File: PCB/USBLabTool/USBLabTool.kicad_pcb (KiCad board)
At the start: 4 copper layers, 79.4 x 56.2 mm, 232 parts, among them J1 Conn_01x06_Pin, J10 T_pwm, J11 T_buf, J12 T_buf, J13 ADC2, J14 ADC1, J15 +3.3VA, J16 +3.3VA, J17 2x01, J19 T_N5V, J2 Conn_02x12_Odd_Even, J20 USB_C_Receptacle, J3 T_att, J4 T_att, J5 T_acdc, J6 T_acdc, J7 T_amp, J8 T_amp, J9 T_pwm, K1 G5V-2, K2 G5V-2, Q1 STL11N3LLH6, SW1 SW_Push, U1 AQY284SX, U10 Opamp_Quad, U11 DG403, U12 STM32H562VGTx, U13 r1283, U14 ST1L05APU33R, U15 ST1L05APU33R, U16 LTC1983ES6-5#TRPBF, U17 TCPP01-M12, U18 74HC245, U2 AQY284SX, U20 74HC245, U3 CD74HC4316PWR, U4 LMP7718, U5 CD74HC4316PWR, U6 LMP7718, U7 OPA863, U8 OPA863, U9 Opamp_Quad, Y1 32.768kHz

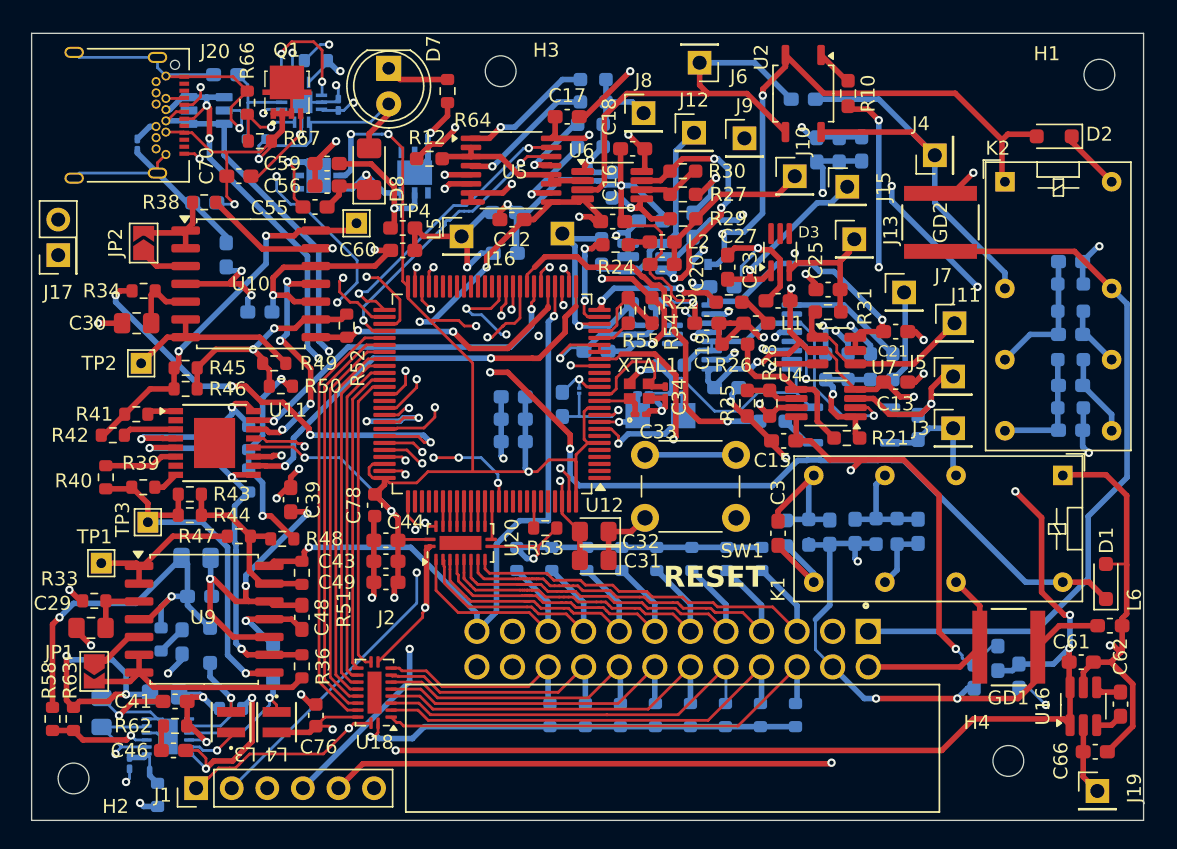
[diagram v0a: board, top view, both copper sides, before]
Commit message: fix footprint and change button
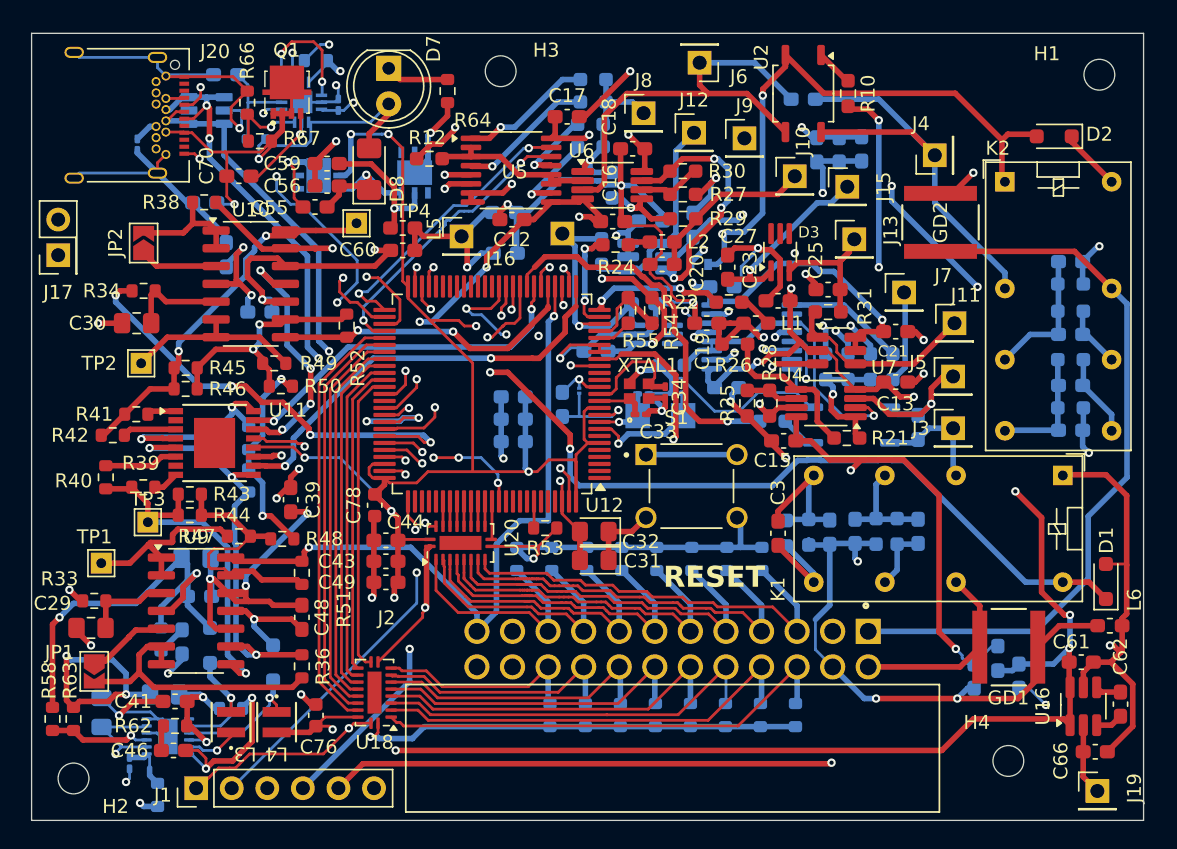
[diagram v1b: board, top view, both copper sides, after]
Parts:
- removed SW1: SW_Push, Button_Switch_THT:SW_PUSH_6mm_H7.3mm
- added S1: TS02-66-73-BK-100-SCR-D, userfp:SW_TS02-66-73-BK-100-SCR-D, F.Cu at (157.1, 97.9)
- U10, U9: footprint Package_SO:SOIC-14W_7.5x9mm_P1.27mm -> Package_SO:SOIC-14_3.9x8.7mm_P1.27mm
- moved U9 0.83 mm to (121.8, 106.8)
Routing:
- net Net-(U9D--): track 13.8 -> 19.0 mm
- net Net-(JP1-B): track 17.1 -> 20.2 mm
- net DAC1_OUT1: track 47.0 -> 49.7 mm
- net +12VA: track 82.3 -> 84.5 mm
- net DAC1_OUT2: track 45.9 -> 48.1 mm
- net Net-(U10B-+): track 4.92 -> 7.10 mm
- net /AWG_FrontEnd/C1_IN: track 3.38 -> 5.56 mm
- net /AWG_FrontEnd/C0_FB: track 28.2 -> 30.3 mm
- net Net-(JP2-B): track 6.56 -> 8.44 mm
- net /AWG_FrontEnd/C0_V_OFF: track 11.2 -> 13.1 mm
- net /AWG_FrontEnd/C0_IN: track 3.92 -> 5.77 mm
- net Net-(U9A-+): track 4.33 -> 6.17 mm
- net GND: track 307.7 -> 309.5 mm
- net -12VA: track 74.5 -> 75.3 mm
- net Net-(U10C--): track 16.9 -> 17.7 mm
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
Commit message: PCB updates from meeting 3/19
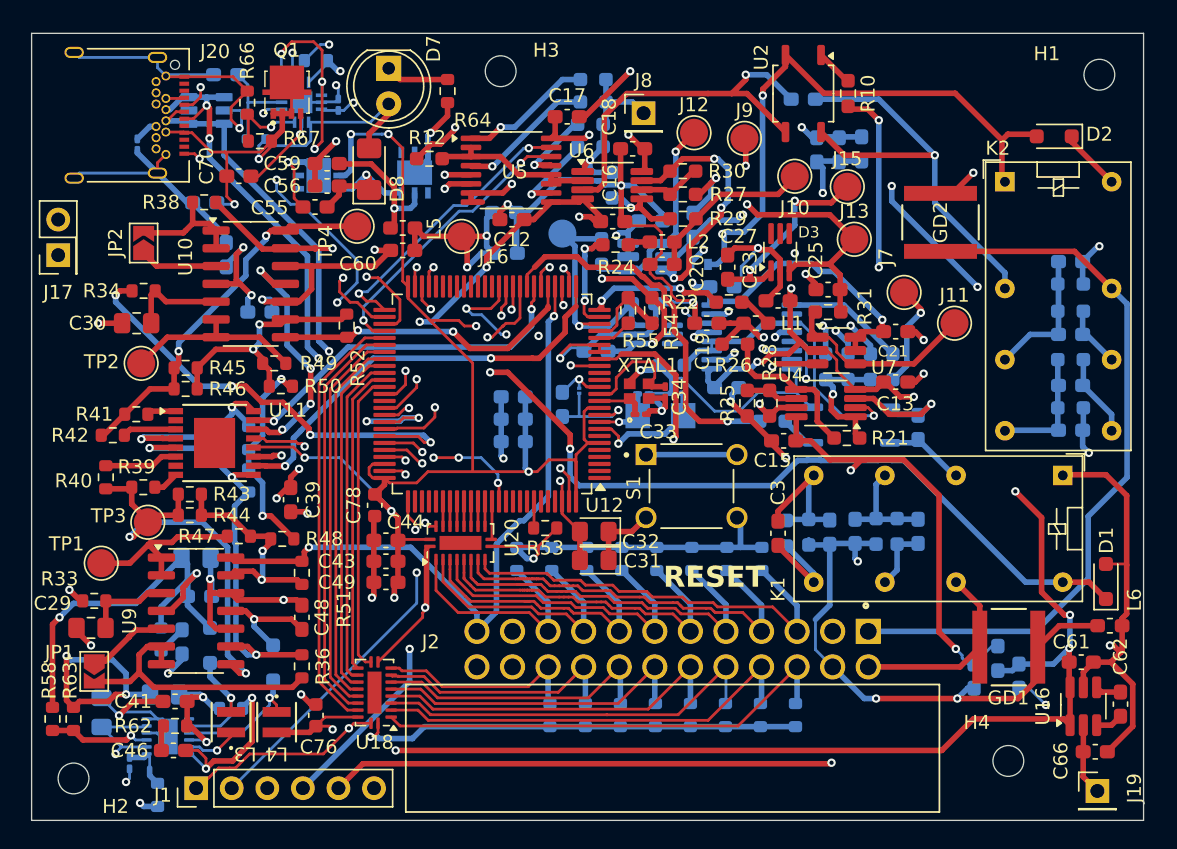
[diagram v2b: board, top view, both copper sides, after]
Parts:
- removed J3, J4: T_att, Connector_PinHeader_2.54mm:PinHeader_1x01_P2.54mm_Vertical
- removed J5, J6: T_acdc, Connector_PinHeader_2.54mm:PinHeader_1x01_P2.54mm_Vertical
- J10, J11, J12, J13, J14, J15, J16, J7, J9: footprint Connector_PinHeader_2.54mm:PinHeader_1x01_P2.54mm_Vertical -> TestPoint:TestPoint_Pad_D2.0mm
- TP1, TP2, TP3, TP4: footprint TestPoint:TestPoint_THTPad_1.5x1.5mm_Drill0.7mm -> TestPoint:TestPoint_Pad_D2.0mm
- moved TP4 0.22 mm to (133.2, 79.3)
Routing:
- net Net-(U6-+IN_A): track 31.3 -> 27.0 mm, vias 0 -> 1
- net UCPD_CC2: track 54.0 -> 49.7 mm, vias 3 -> 4
- net GNDA: track 306.7 -> 302.7 mm
- net +3.3VA: track 57.0 -> 60.3 mm, vias 4 -> 6
- net /AWG_FrontEnd/C0_OUT_G: track 26.3 -> 29.6 mm, vias 1 -> 2
- net Net-(U9D--): track 19.0 -> 15.9 mm, vias 0 -> 2
- net Net-(U4-+IN_A): track 12.7 -> 9.72 mm
- net Net-(C9-Pad1): track 8.39 -> 6.08 mm
- net Net-(J9-Pin_1): track 22.9 -> 21.4 mm, vias 1 -> 2
- net DAC1_OUT1: track 49.7 -> 48.7 mm
- net Net-(J7-Pin_1): track 17.4 -> 18.4 mm, vias 1 -> 2
- net ADC2_INP3: track 39.7 -> 38.9 mm, vias 1 -> 2
- net /AWG_FrontEnd/C0_V_OFF: track 13.1 -> 12.4 mm
- net Net-(J12-Pin_1): track 14.5 -> 14.6 mm, vias 0 -> 1
- net Net-(C10-Pad1): vias 0 -> 1

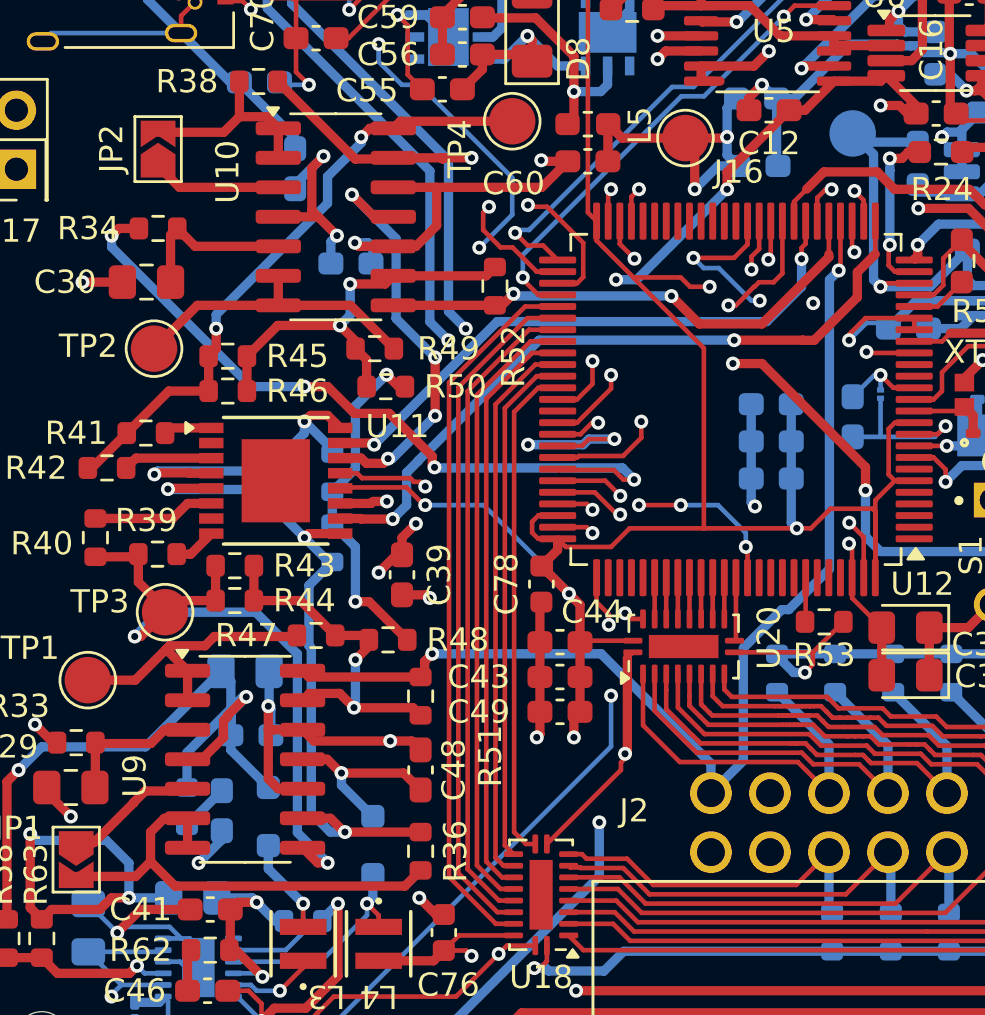
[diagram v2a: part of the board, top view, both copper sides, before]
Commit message: fixed AWG pins to MCU
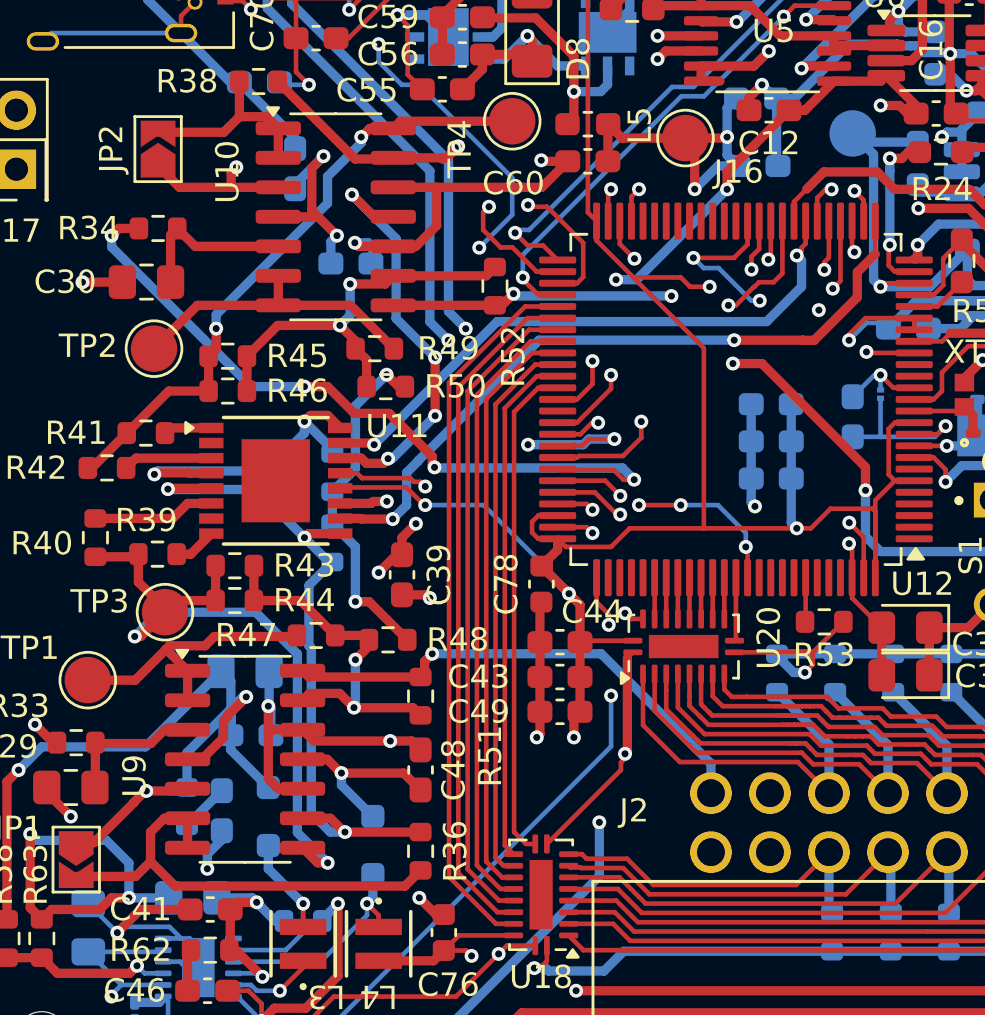
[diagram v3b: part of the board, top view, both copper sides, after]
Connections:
- JP1 pad 1: /AWG_FrontEnd/C0_IN -> C0_IN
- JP2 pad 1: /AWG_FrontEnd/C1_IN -> C1_IN
- U10 pad 3: /AWG_FrontEnd/C1_IN -> C1_IN
- U12 pad 29: DAC1_OUT1 -> C0_IN
- U12 pad 30: DAC1_OUT2 -> C1_IN
- U9 pad 5: /AWG_FrontEnd/C0_IN -> C0_IN
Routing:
- net C0_IN: track 0.00 -> 51.9 mm, vias 0 -> 2
- net C1_IN: track 0.00 -> 36.2 mm, vias 0 -> 2
- net DAC1_OUT1: track 48.7 -> 21.6 mm, vias 2 -> 1
- net DAC1_OUT2: track 48.1 -> 38.1 mm
- net /AWG_FrontEnd/C0_IN: track 5.77 -> 0.00 mm
- net /AWG_FrontEnd/C1_IN: track 5.56 -> 0.00 mm

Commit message: fix parameters
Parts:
- moved Q1 0.55 mm to (128.2, 69.2)
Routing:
- net UCPD_CC2: track 49.7 -> 51.4 mm
- net GNDA: track 302.7 -> 304.0 mm
- net USCPD_DBn: track 37.0 -> 37.7 mm
- net Net-(Q1-G): track 7.12 -> 7.70 mm
- net +5V: track 240.2 -> 240.7 mm

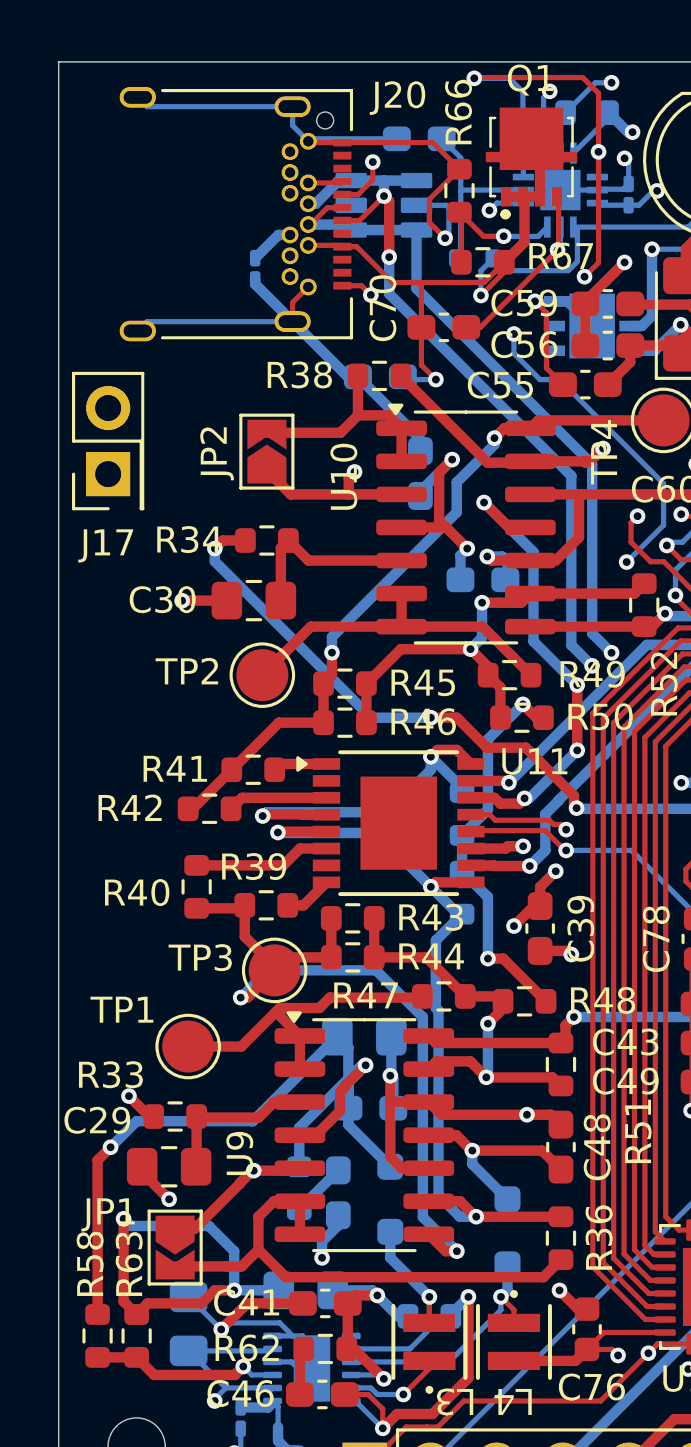
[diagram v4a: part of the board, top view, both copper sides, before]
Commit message: change USB footprint, fix some warnings and problems
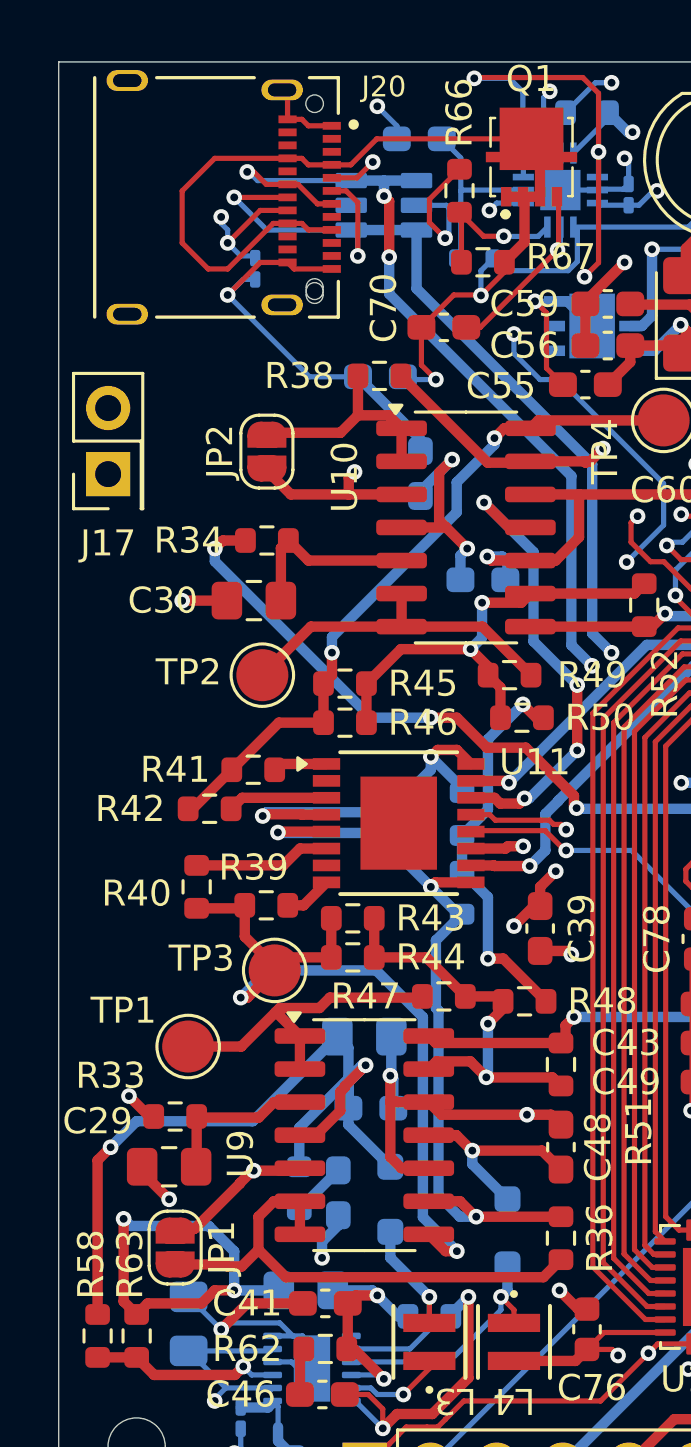
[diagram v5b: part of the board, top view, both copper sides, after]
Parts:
- J20: footprint Connector_USB:USB_C_Receptacle_Amphenol_12401548E4-2A -> userfp:AMPHENOL_12401832E402A
- JP1, JP2: footprint Jumper:SolderJumper-2_P1.3mm_Open_TrianglePad1.0x1.5mm -> Jumper:SolderJumper-2_P1.3mm_Open_RoundedPad1.0x1.5mm
- moved J20 4.01 mm to (119.8, 70.8)
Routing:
- net GND: track 309.5 -> 294.4 mm, vias 30 -> 31
- net +5V: track 240.7 -> 251.5 mm
- net D+: track 38.1 -> 46.2 mm, vias 2 -> 4
- net D-: track 42.2 -> 46.0 mm, vias 4 -> 5
- net UCPD_CC2: track 51.4 -> 52.2 mm, vias 4 -> 6
